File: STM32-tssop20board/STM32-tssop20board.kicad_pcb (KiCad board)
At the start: 2 copper layers, 19.2 x 53.9 mm, 23 parts, among them J1 Conn_01x10_Male, J2 Conn_01x10_Male, J3 Boot0, J4 USB_A, J5 USB_B_Micro, J6 TGT_SWD, J7 IF_SWD, J8 TGT_UART, SW1 Reset, U1 STM32F042F6Px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

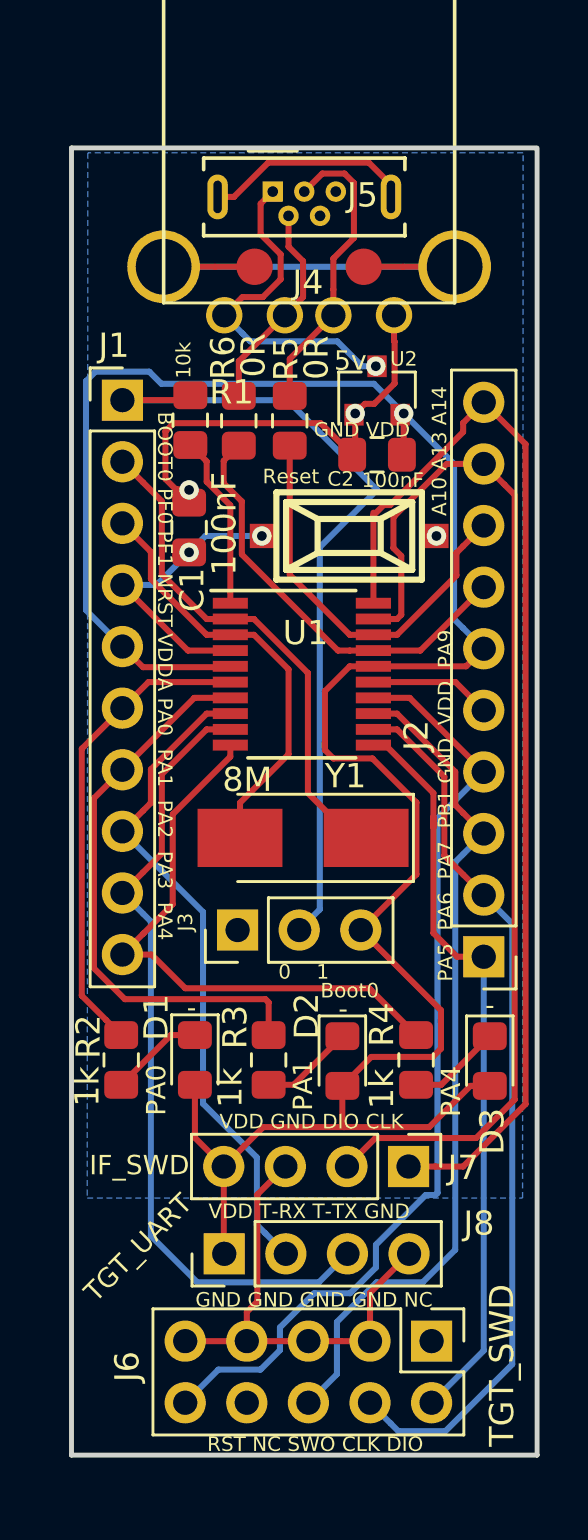
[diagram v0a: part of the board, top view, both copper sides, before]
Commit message: stm32-tssop20board: Fix capacitor for oscillator
Signed-off-by: Zamir SUN <sztsian@gmail.com>
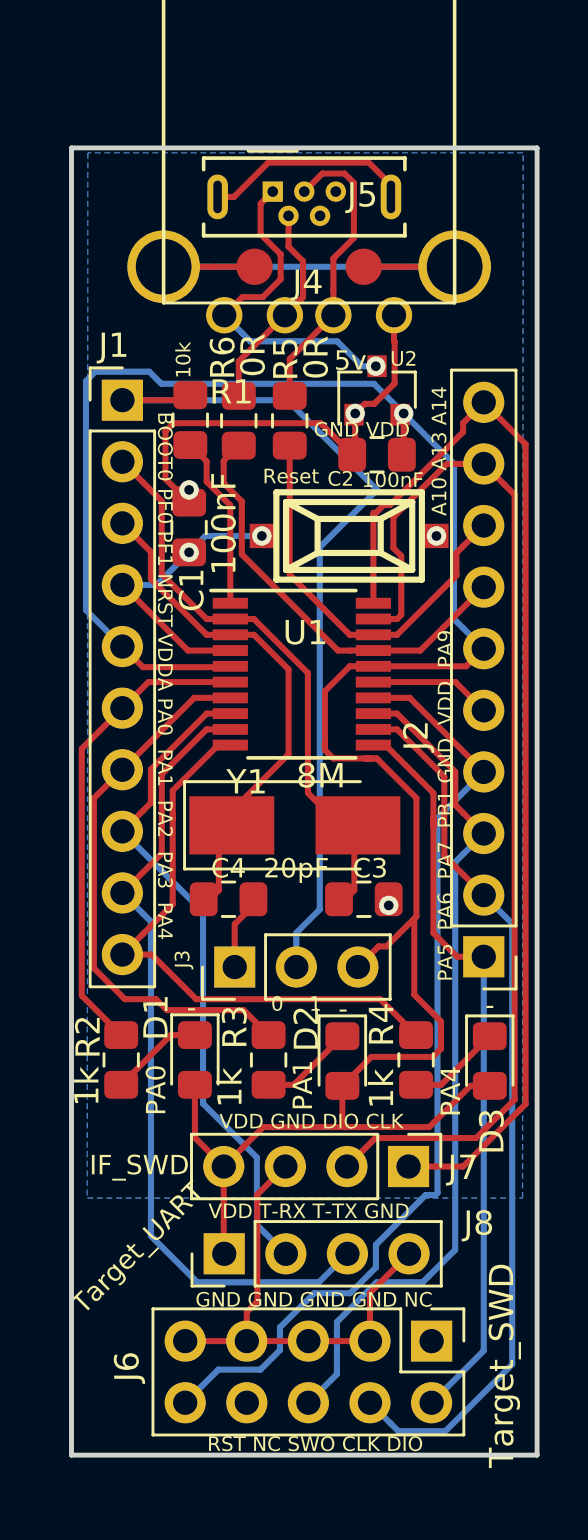
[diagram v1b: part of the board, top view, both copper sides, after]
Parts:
- added C3: 20pF, Capacitor_SMD:C_0805_2012Metric_Pad1.15x1.40mm_HandSolder, F.Cu at (147.1, 81.3)
- added C4: 20pF, Capacitor_SMD:C_0805_2012Metric_Pad1.15x1.40mm_HandSolder, F.Cu at (141.5, 81.3)
- J3: value Boot0 -> Conn_01x03_Male
- J6: value TGT_SWD -> Target_SWD
- J8: value TGT_UART -> Target_UART
- moved J3 1.53 mm to (141.7, 84.1)
- moved Y1 0.62 mm to (144.2, 78.2), turned to 0 degrees
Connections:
- Y1 pad 1: PF0 -> PF1
- Y1 pad 2: PF1 -> PF0
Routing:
- net PF1: track 17.8 -> 21.0 mm
- net GND: track 43.0 -> 45.9 mm, vias 3 -> 4
- net PF0: track 21.7 -> 24.3 mm
- net Boot0: track 34.7 -> 36.3 mm
- net VDD: track 97.0 -> 98.6 mm
- net PA1: track 23.6 -> 22.8 mm

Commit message: Update for some staged changes. Not sure what has changed actually
Signed-off-by: Zamir SUN <sztsian@gmail.com>
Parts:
- moved J4 85.4 mm to (65.8, 34.8), turned to 270 degrees
- moved J5 83.5 mm to (60.7, 39.8), turned to 90 degrees
- moved U2 82.5 mm to (68.9, 35.5), turned to 180 degrees
- moved C2 80.8 mm to (71.6, 35.5), turned to 270 degrees
- moved D3 79.7 mm to (96.6, 30.9), turned to 0 degrees
- moved J2 79.5 mm to (92.3, 31.1), turned to 270 degrees
- moved J6 78.3 mm to (108.1, 33.3), turned to 0 degrees
- moved SW1 77.4 mm to (74.9, 36.7), turned to 270 degrees
- moved R5 77.1 mm to (70.2, 39.1), turned to 180 degrees
- moved R4 75.4 mm to (96.5, 33.9), turned to 0 degrees
- moved J7 75.3 mm to (100.9, 34.2), turned to 0 degrees
- moved R6 74.5 mm to (70.2, 41.2), turned to 180 degrees
- moved C3 72.9 mm to (89.9, 36.1), turned to 90 degrees
- moved R1 72.1 mm to (70.2, 43.2), turned to 0 degrees
- moved U1 72.1 mm to (80.6, 38.6), turned to 90 degrees
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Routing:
- net GND: track 45.9 -> 52.3 mm
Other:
- board size 19.2 x 53.9 mm -> 53.9 x 19.2 mm
